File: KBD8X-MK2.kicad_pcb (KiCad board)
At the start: 2 copper layers, 343.7 x 118.3 mm, 215 parts, among them J1 AVR-ISP-6, Q1 DSS60601MZ4-13, SW1 SW_Push, U1 ATmega32U4-MU, U2 PRTR5V0U2X, Y1 16MHz

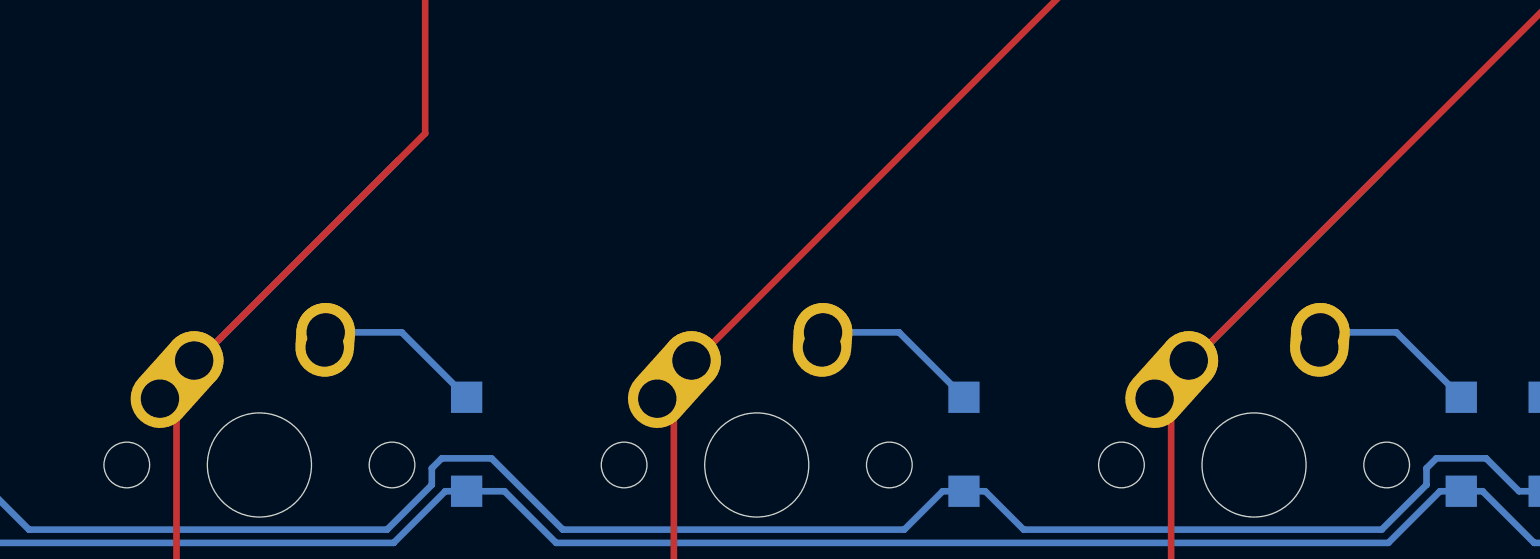
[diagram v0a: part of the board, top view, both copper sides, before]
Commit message: update image + remove unrouted row 2 traces
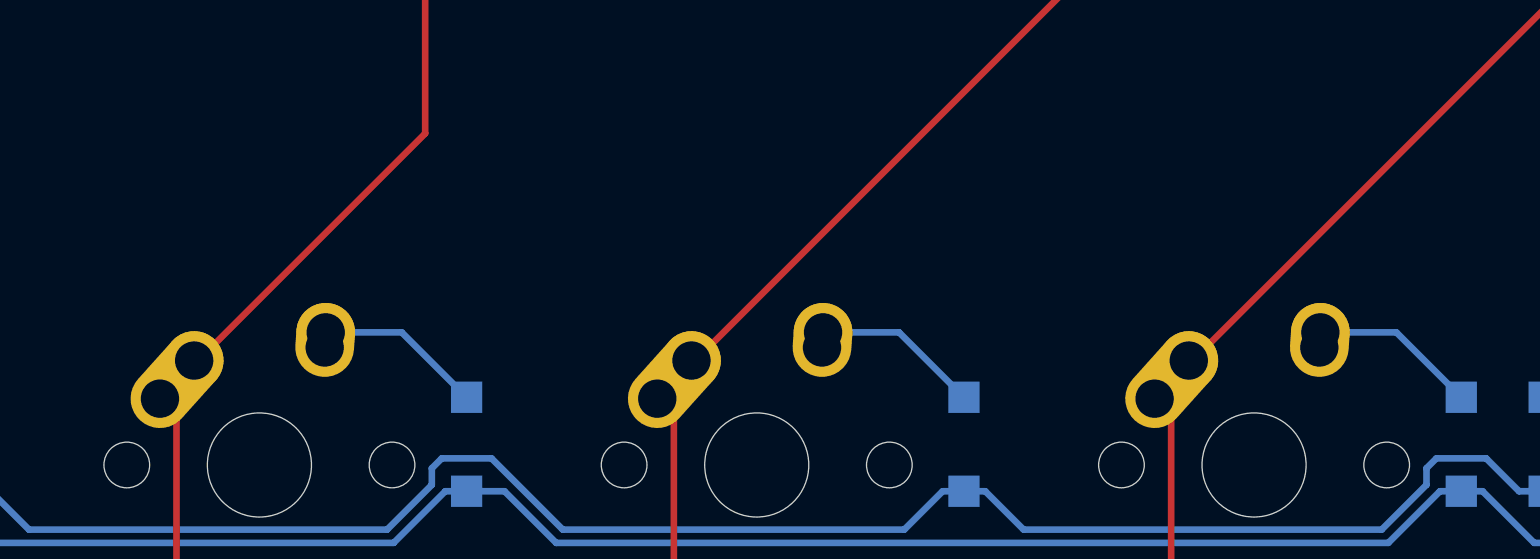
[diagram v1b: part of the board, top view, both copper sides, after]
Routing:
- net COL4: track 357.5 -> 344.5 mm
- net COL5: track 331.7 -> 319.5 mm
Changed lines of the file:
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@@
   (segment (start 286.639 72.009) (end 286.004 71.374) (width 0.254) (layer "F.Cu") (net 104))
   (segment (start 215.265 60.96) (end 225.425 50.8) (width 0.254) (layer "F.Cu") (net 104))
-  (segment (start 224.409 51.816) (end 215.265 60.96) (width 0.254) (layer "B.Cu") (net 104))
   (segment (start 258.1275 118.11) (end 258.699 118.6815) (width 0.254) (layer "F.Cu") (net 105))
   (segment (start 234.95 68.834) (end 234.95 61.595) (width 0.254) (layer "F.Cu") (net 105))
@@
   (segment (start 248.6025 99.06) (end 248.6025 97.4725) (width 0.254) (layer "F.Cu") (net 105))
   (segment (start 254 37.7825) (end 253.365 37.1475) (width 0.254) (layer "F.Cu") (net 105))
-  (segment (start 262.001 52.324) (end 253.365 60.96) (width 0.254) (layer "B.Cu") (net 105))
   (segment (start 311.15 41.275) (end 311.15 37.7825) (width 0.254) (layer "F.Cu") (net 106))
   (segment (start 292.1 41.275) (end 292.1 37.7825) (width 0.254) (layer "F.Cu") (net 106))

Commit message: mx alps 2.75u shift, trim + prettify pcb
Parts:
- removed C2: 1uF, locallib:C_0603
- removed C5: 10uF, locallib:C_0603
- removed F1: 500mA, Fuse_Holders_and_Fuses:Fuse_SMD1206_Wave
- removed RC4: 1k, locallib:R_0603
- removed RC6, RC7: 5k1, locallib:R_0603
- MX_RSHIFT1: footprint MX_Alps_Hybrid:MXOnly-2.75U -> MX_Alps_Hybrid:MX-2.75U-NoLED
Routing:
- net Net-(RC6-Pad2): track 6.15 -> 0.00 mm, vias 2 -> 0
- net VCC: track 17.0 -> 11.1 mm
- net Net-(RC7-Pad2): track 5.57 -> 0.00 mm, vias 2 -> 0
- net Net-(C2-Pad1): track 4.56 -> 0.00 mm
- net Net-(RC4-Pad1): track 3.88 -> 0.00 mm
- net Net-(D31-Pad2): track 38.9 -> 41.7 mm
- net COL0: track 203.9 -> 203.2 mm
- net Net-(D78-Pad2): track 16.0 -> 16.6 mm
- net RGBLED: track 43.7 -> 43.1 mm, vias 1 -> 0
- net SLOCK_IND: track 51.8 -> 51.5 mm, vias 1 -> 0

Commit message: clean up stuff
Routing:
- net Net-(D111-Pad2): track 11.5 -> 12.5 mm
- net Net-(D65-Pad2): track 24.5 -> 25.5 mm
- net Net-(D91-Pad2): track 13.9 -> 14.8 mm
- net Net-(D82-Pad2): track 13.9 -> 14.8 mm
- net Net-(D86-Pad2): track 13.9 -> 14.7 mm
- net Net-(D93-Pad2): track 11.5 -> 12.3 mm
- net Net-(D11-Pad2): track 11.5 -> 12.2 mm
- net Net-(D101-Pad2): track 11.5 -> 12.2 mm
- net Net-(D97-Pad2): track 11.5 -> 12.2 mm
- net Net-(D13-Pad2): track 11.5 -> 12.1 mm
- net Net-(D3-Pad2): track 11.5 -> 12.1 mm
- net Net-(D7-Pad2): track 11.5 -> 12.1 mm
- net Net-(D29-Pad2): track 11.5 -> 12.1 mm
- net Net-(D94-Pad2): track 15.3 -> 15.8 mm
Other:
- board text added: "Rogue - ai03 KBD8X-MKII PCB Rev 2.1 20220313"
- board text removed: "KBD8X-MKII PCB Rev 2.0 20190404"

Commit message: add aek support + more documents
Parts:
- added MX_CLOCK2: MX-1.25U, Alps_Only:ALPS-1U, F.Cu at (52.5, 101.6)
- added MX_LALT2: MX-1.5U, Alps_Only:ALPS-1.5U, F.Cu at (104.9, 139.8)
- added MX_LALT2: MX-1.5U, Alps_Only:ALPS-1.5U, F.Cu at (257.1, 139.7)
- added MX_LGUI1: MX-1.25U, Alps_Only:ALPS-1.25U, F.Cu at (283.4, 139.7)
- added MX_LGUI1: MX-1.25U, Alps_Only:ALPS-1.25U, F.Cu at (78.6, 139.8)
- added MX_SP1: MX-6.25U, Alps_Only:ALPS-6.5U, F.Cu at (176.3, 139.8)
- MX_CLOCK2: footprint MX_Alps_Hybrid:MX-1.25U-NoLED -> MX_Only:MXOnly-1U-NoLED
- MX_LALT1, MX_LCTRL1, MX_LGUI1, MX_RALT1, MX_RCTRL1, MX_RGUI1, MX_RMENU1: footprint MX_Alps_Hybrid:MX-1.25U-NoLED -> MX_Only:MXOnly-1.25U-NoLED
- MX_SP1: footprint MX_Alps_Hybrid:MX-6.25U-ReversedStabilizers-NoLED -> MX_Only:MXOnly-6.25U-ReversedStabilizers-NoLED

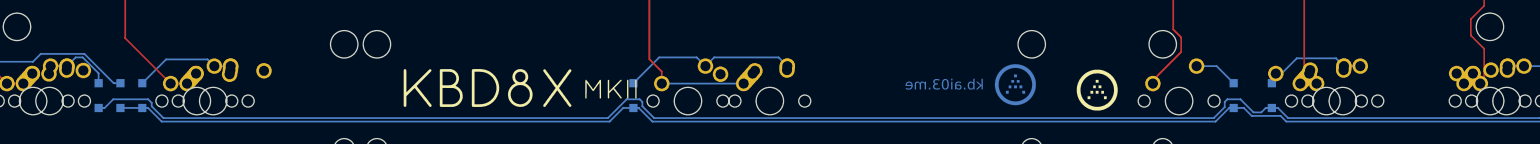
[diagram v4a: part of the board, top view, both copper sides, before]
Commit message: remove aek layout since they're not compatible with 6.25u layout for now
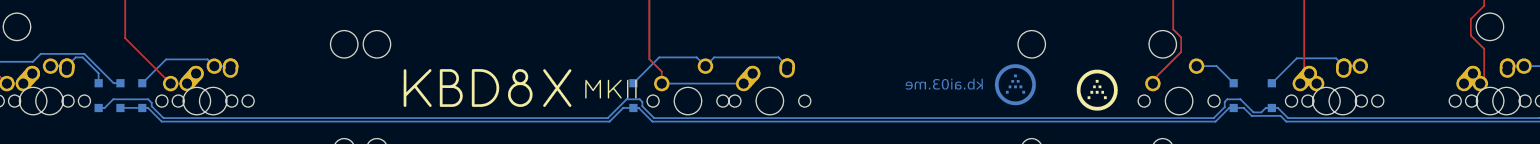
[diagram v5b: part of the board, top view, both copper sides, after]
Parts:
- removed the MX_LALT2 at (104.9, 139.8)
- removed the MX_LALT2 at (257.1, 139.7)
- removed the MX_LGUI1 at (283.4, 139.7)
- removed the MX_LGUI1 at (78.6, 139.8)
- removed the MX_SP1 at (176.3, 139.8)
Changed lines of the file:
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@@
       (net 88 "Net-(D93-Pad2)"))
-  )
-  (footprint "Alps_Only:ALPS-1.5U" (layer "F.Cu")
-    (at 104.896861 139.800118)
-    (attr through_hole)
-    (fp_text reference "MX_LALT2" (at 0 3.175) (layer "Dwgs.User")
-      (effects (font (size 1 1) (thickness 0.15)))
-    )
-    (fp_text value "MX-1.5U" (at 0 -7.9375) (layer "Dwgs.User")
-      (effects (font (size 1 1) (thickness 0.15)))
-    )
-    (fp_line (start -5 -7) (end -7 -7) (layer "Dwgs.User") (width 0.15))
-    (fp_line (start 7 7) (end 7 5) (layer "Dwgs.User") (width 0.15))
-    (fp_line (start 7 -7) (end 7 -5) (layer "Dwgs.User") (width 0.15))
-    (fp_line (start -7 7) (end -5 7) (layer "Dwgs.User") (width 0.15))
-    (fp_line (start -7 -7) (end -7 -5) (layer "Dwgs.User") (width 0.15))
-    (fp_line (start -14.2875 9.525) (end 14.2875 9.525) (layer "Dwgs.User") (width 0.15))
-    (fp_line (start 5 7) (end 7 7) (layer "Dwgs.User") (width 0.15))
-    (fp_line (start -7 5) (end -7 7) (layer "Dwgs.User") (width 0.15))
-    (fp_line (start -14.2875 -9.525) (end 14.2875 -9.525) (layer "Dwgs.User") (width 0.15))
-    (fp_line (start 14.2875 -9.525) (end 14.2875 9.525) (layer "Dwgs.User") (width 0.15))
-    (fp_line (start -14.2875 9.525) (end -14.2875 -9.525) (layer "Dwgs.User") (width 0.15))
-    (fp_line (start 5 -7) (end 7 -7) (layer "Dwgs.User") (width 0.15))
-    (pad "1" thru_hole circle locked (at -2.5 -4) (size 2.25 2.25) (drill 1.47) (layers *.Cu "B.Mask"))
-    (pad "2" thru_hole circle locked (at 2.5 -4.5) (size 2.25 2.25) (drill 1.47) (layers *.Cu "B.Mask"))
-  )
-  (footprint "Alps_Only:ALPS-1.5U" (layer "F.Cu")
-    (at 257.071191 139.701123)
-    (attr through_hole)
-    (fp_text reference "MX_LALT2" (at 0 3.175) (layer "Dwgs.User")
-      (effects (font (size 1 1) (thickness 0.15)))
-    )
-    (fp_text value "MX-1.5U" (at 0 -7.9375) (layer "Dwgs.User")
-      (effects (font (size 1 1) (thickness 0.15)))
-    )
-    (fp_line (start -5 -7) (end -7 -7) (layer "Dwgs.User") (width 0.15))
-    (fp_line (start 7 7) (end 7 5) (layer "Dwgs.User") (width 0.15))
-    (fp_line (start 7 -7) (end 7 -5) (layer "Dwgs.User") (width 0.15))
-    (fp_line (start -7 7) (end -5 7) (layer "Dwgs.User") (width 0.15))
-    (fp_line (start -7 -7) (end -7 -5) (layer "Dwgs.User") (width 0.15))
-    (fp_line (start -14.2875 9.525) (end 14.2875 9.525) (layer "Dwgs.User") (width 0.15))
-    (fp_line (start 5 7) (end 7 7) (layer "Dwgs.User") (width 0.15))
-    (fp_line (start -7 5) (end -7 7) (layer "Dwgs.User") (width 0.15))
-    (fp_line (start -14.2875 -9.525) (end 14.2875 -9.525) (layer "Dwgs.User") (width 0.15))
-    (fp_line (start 14.2875 -9.525) (end 14.2875 9.525) (layer "Dwgs.User") (width 0.15))
-    (fp_line (start -14.2875 9.525) (end -14.2875 -9.525) (layer "Dwgs.User") (width 0.15))
-    (fp_line (start 5 -7) (end 7 -7) (layer "Dwgs.User") (width 0.15))
-    (pad "1" thru_hole circle locked (at -2.5 -4) (size 2.25 2.25) (drill 1.47) (layers *.Cu "B.Mask"))
-    (pad "2" thru_hole circle locked (at 2.5 -4.5) (size 2.25 2.25) (drill 1.47) (layers *.Cu "B.Mask"))
   )
   (footprint "Alps_Only:ALPS-1U" (layer "F.Cu")
@@
     (pad "2" thru_hole circle (at 2.5 -4.5) (size 2.25 2.25) (drill 1.47) (layers *.Cu "B.Mask"))
   )
-  (footprint "Alps_Only:ALPS-1.25U" (layer "F.Cu")
-    (at 283.374332 139.701124)
-    (attr through_hole)
-    (fp_text reference "MX_LGUI1" (at 0 3.175) (layer "Dwgs.User")
-      (effects (font (size 1 1) (thickness 0.15)))
-    )
-    (fp_text value "MX-1.25U" (at 0 -7.9375) (layer "Dwgs.User")
-      (effects (font (size 1 1) (thickness 0.15)))
-    )
-    (fp_line (start 11.90625 -9.525) (end 11.90625 9.525) (layer "Dwgs.User") (width 0.15))
-    (fp_line (start -11.90625 -9.525) (end 11.90625 -9.525) (layer "Dwgs.User") (width 0.15))
-    (fp_line (start -11.90625 9.525) (end -11.90625 -9.525) (layer "Dwgs.User") (width 0.15))
-    (fp_line (start -11.90625 9.525) (end 11.90625 9.525) (layer "Dwgs.User") (width 0.15))
-    (fp_line (start 5 -7) (end 7 -7) (layer "Dwgs.User") (width 0.15))
-    (fp_line (start 5 7) (end 7 7) (layer "Dwgs.User") (width 0.15))
-    (fp_line (start 7 -7) (end 7 -5) (layer "Dwgs.User") (width 0.15))
-    (fp_line (start -5 -7) (end -7 -7) (layer "Dwgs.User") (width 0.15))
-    (fp_line (start -7 7) (end -5 7) (layer "Dwgs.User") (width 0.15))
-    (fp_line (start 7 7) (end 7 5) (layer "Dwgs.User") (width 0.15))
-    (fp_line (start -7 5) (end -7 7) (layer "Dwgs.User") (width 0.15))
-    (fp_line (start -7 -7) (end -7 -5) (layer "Dwgs.User") (width 0.15))
-    (pad "1" thru_hole circle locked (at -2.5 -4) (size 2.25 2.25) (drill 1.47) (layers *.Cu "B.Mask"))
-    (pad "2" thru_hole circle locked (at 2.5 -4.5) (size 2.25 2.25) (drill 1.47) (layers *.Cu "B.Mask"))
-  )
-  (footprint "Alps_Only:ALPS-1.25U" (layer "F.Cu")
-    (at 78.622193 139.752228)
-    (attr through_hole)
-    (fp_text reference "MX_LGUI1" (at 0 3.175) (layer "Dwgs.User")
-      (effects (font (size 1 1) (thickness 0.15)))
-    )
-    (fp_text value "MX-1.25U" (at 0 -7.9375) (layer "Dwgs.User")
-      (effects (font (size 1 1) (thickness 0.15)))
-    )
-    (fp_line (start 11.90625 -9.525) (end 11.90625 9.525) (layer "Dwgs.User") (width 0.15))
-    (fp_line (start -11.90625 -9.525) (end 11.90625 -9.525) (layer "Dwgs.User") (width 0.15))
-    (fp_line (start -11.90625 9.525) (end -11.90625 -9.525) (layer "Dwgs.User") (width 0.15))
-    (fp_line (start -11.90625 9.525) (end 11.90625 9.525) (layer "Dwgs.User") (width 0.15))
-    (fp_line (start 5 -7) (end 7 -7) (layer "Dwgs.User") (width 0.15))
-    (fp_line (start 5 7) (end 7 7) (layer "Dwgs.User") (width 0.15))
-    (fp_line (start 7 -7) (end 7 -5) (layer "Dwgs.User") (width 0.15))
-    (fp_line (start -5 -7) (end -7 -7) (layer "Dwgs.User") (width 0.15))
-    (fp_line (start -7 7) (end -5 7) (layer "Dwgs.User") (width 0.15))
-    (fp_line (start 7 7) (end 7 5) (layer "Dwgs.User") (width 0.15))
-    (fp_line (start -7 5) (end -7 7) (layer "Dwgs.User") (width 0.15))
-    (fp_line (start -7 -7) (end -7 -5) (layer "Dwgs.User") (width 0.15))
-    (pad "1" thru_hole circle locked (at -2.5 -4) (size 2.25 2.25) (drill 1.47) (layers *.Cu "B.Mask"))
-    (pad "2" thru_hole circle locked (at 2.5 -4.5) (size 2.25 2.25) (drill 1.47) (layers *.Cu "B.Mask"))
-  )
-  (footprint "Alps_Only:ALPS-6.5U" (layer "F.Cu")
-    (at 176.306546 139.799165)
-    (attr through_hole)
-    (fp_text reference "MX_SP1" (at 0 3.175) (layer "Dwgs.User")
-      (effects (font (size 1 1) (thickness 0.15)))
-    )
-    (fp_text value "MX-6.25U" (at 0 -7.9375) (layer "Dwgs.User")
-      (effects (font (size 1 1) (thickness 0.15)))
-    )
-    (fp_line (start 5 -7) (end 7 -7) (layer "Dwgs.User") (width 0.15))
-    (fp_line (start 61.9125 -9.525) (end 61.9125 9.525) (layer "Dwgs.User") (width 0.15))
-    (fp_line (start -61.9125 -9.525) (end 61.9125 -9.525) (layer "Dwgs.User") (width 0.15))
-    (fp_line (start 5 7) (end 7 7) (layer "Dwgs.User") (width 0.15))
-    (fp_line (start -7 7) (end -5 7) (layer "Dwgs.User") (width 0.15))
-    (fp_line (start -61.9125 9.525) (end 61.9125 9.525) (layer "Dwgs.User") (width 0.15))
-    (fp_line (start -7 5) (end -7 7) (layer "Dwgs.User") (width 0.15))
-    (fp_line (start -61.9125 9.525) (end -61.9125 -9.525) (layer "Dwgs.User") (width 0.15))
-    (fp_line (start -7 -7) (end -7 -5) (layer "Dwgs.User") (width 0.15))
-    (fp_line (start 7 7) (end 7 5) (layer "Dwgs.User") (width 0.15))
-    (fp_line (start -5 -7) (end -7 -7) (layer "Dwgs.User") (width 0.15))
-    (fp_line (start 7 -7) (end 7 -5) (layer "Dwgs.User") (width 0.15))
-    (pad "1" thru_hole circle locked (at -2.5 -4) (size 2.25 2.25) (drill 1.47) (layers *.Cu "B.Mask"))
-    (pad "2" thru_hole circle locked (at 2.5 -4.5) (size 2.25 2.25) (drill 1.47) (layers *.Cu "B.Mask"))
-  )
   (footprint "TO_SOT_Packages_SMD:SOT-223-3_TabPin2" (layer "B.Cu")
